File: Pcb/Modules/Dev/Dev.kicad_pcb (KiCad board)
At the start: 2 copper layers, 50.8 x 20.3 mm, 6 parts, among them J1 JACK_STEREO, J2 JACK_RJ45, P1 CONN_02X04, Q1 Q_NMOS_GSD, SW0 SW_TACTILE

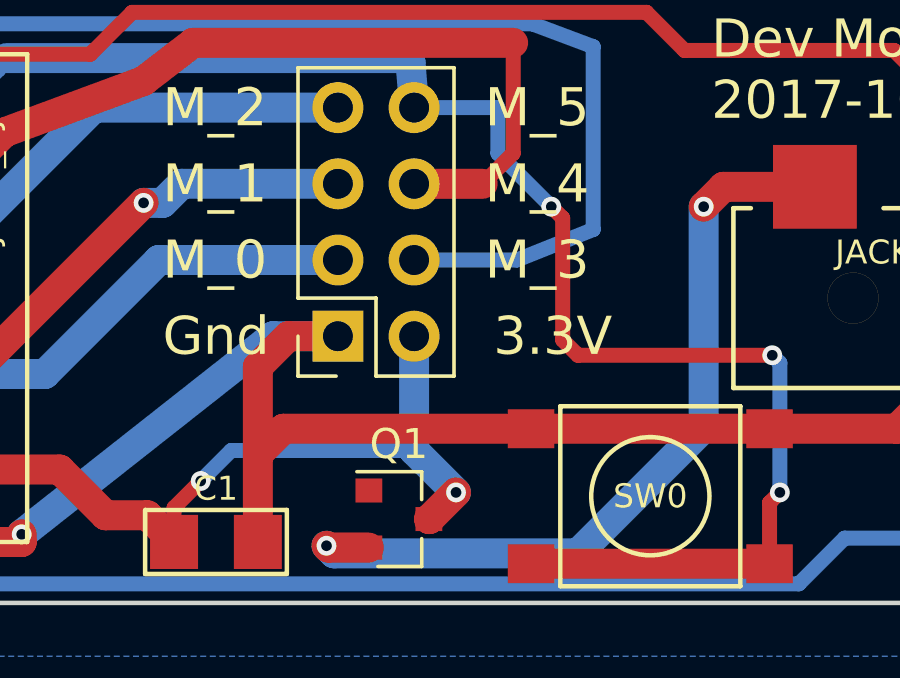
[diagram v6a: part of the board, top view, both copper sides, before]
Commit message: Fix missing wire on dev board and stop rounding corners on light pcb
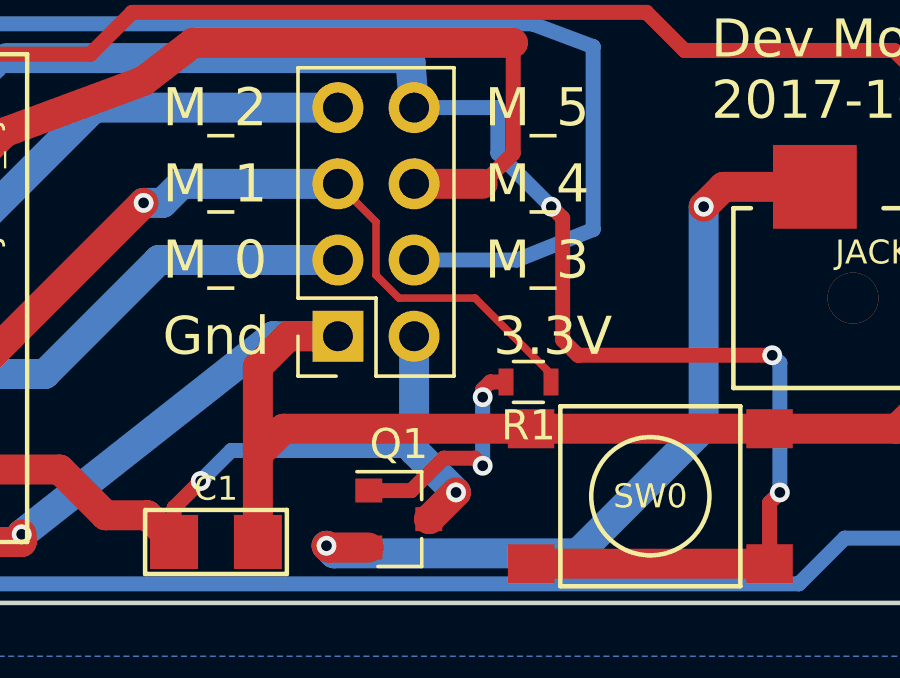
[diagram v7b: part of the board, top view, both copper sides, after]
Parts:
- added R1: 1K, Resistors_SMD:R_0603, F.Cu at (54.6, 38.4)
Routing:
- net /M_1: track 30.4 -> 41.4 mm
- net Net-(Q1-Pad1): track 0.00 -> 7.77 mm, vias 0 -> 2
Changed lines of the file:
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@@
 (kicad_pcb (version 4) (host pcbnew 4.0.5)
   (general
-    (links 20)
+    (links 22)
     (no_connects 0)
-    (area 21.873869 24.13 78.740001 48.768001)
+    (area 25.324999 25.324999 76.275001 45.795001)
     (thickness 1.6)
     (drawings 21)
-    (tracks 137)
+    (tracks 153)
     (zones 0)
-    (modules 6)
+    (modules 7)
     (nets 11)
   )
@@
   )
   (setup
-    (last_trace_width 0.5)
+    (last_trace_width 0.254)
+    (user_trace_width 0.254)
     (trace_clearance 0.2032)
     (zone_clearance 0.508)
@@
     (pad 4 smd rect (at 3.975 2.25) (size 1.55 1.3) (layers F.Cu F.Paste F.Mask)
       (net 9 /M_5))
+  )
+  (module Resistors_SMD:R_0603 (layer F.Cu)
+    (at 54.61 38.354 180)
+    (descr "Resistor SMD 0603, reflow soldering, Vishay (see dcrcw.pdf)")
+    (tags "resistor 0603")
+    (attr smd)
+    (fp_text reference R1 (at 0 -1.45 180) (layer F.SilkS)
+      (effects (font (size 1 1) (thickness 0.15)))
+    )
+    (fp_text value 1K (at 0 1.5 180) (layer F.Fab)
+      (effects (font (size 1 1) (thickness 0.15)))
+    )
+    (fp_text user %R (at 0 0 180) (layer F.Fab)
+      (effects (font (size 0.4 0.4) (thickness 0.075)))
+    )
+    (fp_line (start -0.8 0.4) (end -0.8 -0.4) (layer F.Fab) (width 0.1))
+    (fp_line (start 0.8 0.4) (end -0.8 0.4) (layer F.Fab) (width 0.1))
+    (fp_line (start 0.8 -0.4) (end 0.8 0.4) (layer F.Fab) (width 0.1))
+    (fp_line (start -0.8 -0.4) (end 0.8 -0.4) (layer F.Fab) (width 0.1))
+    (fp_line (start 0.5 0.68) (end -0.5 0.68) (layer F.SilkS) (width 0.12))
+    (fp_line (start -0.5 -0.68) (end 0.5 -0.68) (layer F.SilkS) (width 0.12))
+    (fp_line (start -1.25 -0.7) (end 1.25 -0.7) (layer F.CrtYd) (width 0.05))
+    (fp_line (start -1.25 -0.7) (end -1.25 0.7) (layer F.CrtYd) (width 0.05))
+    (fp_line (start 1.25 0.7) (end 1.25 -0.7) (layer F.CrtYd) (width 0.05))
+    (fp_line (start 1.25 0.7) (end -1.25 0.7) (layer F.CrtYd) (width 0.05))
+    (pad 1 smd rect (at -0.75 0 180) (size 0.5 0.9) (layers F.Cu F.Paste F.Mask)
+      (net 6 /M_1))
+    (pad 2 smd rect (at 0.75 0 180) (size 0.5 0.9) (layers F.Cu F.Paste F.Mask)
+      (net 10 "Net-(Q1-Pad1)"))
+    (model ${KISYS3DMOD}/Resistors_SMD.3dshapes/R_0603.wrl
+      (at (xyz 0 0 0))
+      (scale (xyz 1 1 1))
+      (rotate (xyz 0 0 0))
+    )
   )
   (gr_line (start 76.2 25.4) (end 76.2 31.75) (angle 90) (layer Edge.Cuts) (width 0.15))
@@
   (segment (start 26.797 34.941) (end 26.797 32.258) (width 0.5) (layer F.Cu) (net 5))
   (segment (start 26.678 35.06) (end 26.797 34.941) (width 0.5) (layer F.Cu) (net 5))
-  (segment (start 30.099 41.783) (end 29.845 41.783) (width 0.5) (layer B.Cu) (net 6))
+  (segment (start 55.36 38.354) (end 55.36 38.088) (width 0.254) (layer F.Cu) (net 6))
+  (segment (start 55.36 38.088) (end 52.832 35.56) (width 0.254) (layer F.Cu) (net 6))
+  (segment (start 52.832 35.56) (end 50.292 35.56) (width 0.254) (layer F.Cu) (net 6))
+  (segment (start 50.292 35.56) (end 49.53 34.798) (width 0.254) (layer F.Cu) (net 6))
+  (segment (start 49.53 34.798) (end 49.53 33.02) (width 0.254) (layer F.Cu) (net 6))
+  (segment (start 49.53 33.02) (end 48.26 31.75) (width 0.254) (layer F.Cu) (net 6))
+  (segment (start 48.26 31.75) (end 43.053 31.75) (width 1) (layer B.Cu) (net 6) (status 10))
   (segment (start 43.053 31.75) (end 42.418 32.385) (width 1) (layer B.Cu) (net 6))
   (segment (start 42.418 32.385) (end 41.783 32.385) (width 1) (layer B.Cu) (net 6))
   (via (at 41.783 32.385) (size 0.6604) (drill 0.3556) (layers F.Cu B.Cu) (net 6))
   (segment (start 41.783 32.385) (end 34.671 39.497) (width 1) (layer F.Cu) (net 6))
+  (segment (start 30.099 41.783) (end 29.845 41.783) (width 0.5) (layer B.Cu) (net 6))
   (via (at 34.671 39.497) (size 0.6604) (drill 0.3556) (layers F.Cu B.Cu) (net 6))
   (segment (start 34.671 39.497) (end 32.385 41.783) (width 1) (layer B.Cu) (net 6))
   (segment (start 32.385 41.783) (end 30.099 41.783) (width 1) (layer B.Cu) (net 6))
-  (segment (start 48.26 31.75) (end 43.053 31.75) (width 1) (layer B.Cu) (net 6) (status 10))
   (segment (start 27.819 37.09) (end 30.092 37.09) (width 0.5) (layer F.Cu) (net 6) (status 20))
   (segment (start 27.813 37.084) (end 27.819 37.09) (width 0.5) (layer F.Cu) (net 6))
@@
   (segment (start 50.546 27.559) (end 37.211 27.559) (width 1) (layer B.Cu) (net 9))
   (segment (start 62.649 44.414) (end 54.699 44.414) (width 1) (layer F.Cu) (net 9) (status 30))
+  (segment (start 53.086 38.862) (end 53.086 38.608) (width 0.5) (layer F.Cu) (net 10))
+  (segment (start 49.292 41.976) (end 50.707202 41.976) (width 0.5) (layer F.Cu) (net 10))
+  (via (at 53.086 38.862) (size 0.6604) (drill 0.3556) (layers F.Cu B.Cu) (net 10))
+  (segment (start 53.086 41.148) (end 53.086 38.862) (width 0.5) (layer B.Cu) (net 10))
+  (via (at 53.086 41.148) (size 0.6604) (drill 0.3556) (layers F.Cu B.Cu) (net 10))
+  (segment (start 52.832 40.894) (end 53.086 41.148) (width 0.5) (layer F.Cu) (net 10))
+  (segment (start 51.789202 40.894) (end 52.832 40.894) (width 0.5) (layer F.Cu) (net 10))
+  (segment (start 50.707202 41.976) (end 51.789202 40.894) (width 0.5) (layer F.Cu) (net 10))
+  (segment (start 53.34 38.354) (end 53.86 38.354) (width 0.5) (layer F.Cu) (net 10))
+  (segment (start 53.086 38.608) (end 53.34 38.354) (width 0.5) (layer F.Cu) (net 10))
   (zone (net 2) (net_name GND) (layer F.Cu) (hatch edge 0.508)
     (connect_pads (clearance 0.508))

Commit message: Update PCBs
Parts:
- added R2: 10K, Resistors_SMD:R_0603, F.Cu at (64.8, 43.8)
- added X1: HOLE, Mounting_Holes:MountingHole_2.5mm_Pad, F.Cu at (41.3, 28.6)
- added X2: HOLE, Mounting_Holes:MountingHole_2.5mm_Pad, F.Cu at (41.3, 42.5)
- added X3: HOLE, Mounting_Holes:MountingHole_2.5mm_Pad, F.Cu at (60.3, 28.6)
- added X4: HOLE, Mounting_Holes:MountingHole_2.5mm_Pad, F.Cu at (60.3, 42.5)
- C1: value C -> 10uF
- moved Q1 17.7 mm to (67.9, 42.5)
- moved R1 10.4 mm to (64.8, 40.6), turned to 0 degrees
- moved SW0 7.92 mm to (50.8, 41.3), turned to 180 degrees
- moved C1 6.63 mm to (41.9, 37.5)
- moved P1 2.29 mm to (49.5, 34.9)
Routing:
- net GND: track 113.7 -> 6.63 mm, vias 1 -> 5
- net /M_3: track 52.8 -> 29.3 mm, vias 1 -> 4
- net 3V3: track 32.0 -> 49.0 mm, vias 2 -> 0
- net /M_0: track 63.2 -> 46.6 mm, vias 1 -> 0
- net /M_5: track 59.5 -> 43.6 mm, vias 3 -> 4
- net /M_1: track 41.4 -> 54.1 mm, vias 3 -> 2
- net /M_4: track 32.1 -> 23.0 mm, vias 0 -> 2
- net Net-(Q1-Pad1): track 7.77 -> 1.82 mm, vias 2 -> 0
- net Net-(J1-Pad2): track 27.2 -> 25.0 mm, vias 2 -> 0
- net /M_2: track 20.2 -> 21.3 mm
- removed copper zone on F.Cu, net GND
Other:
- net class Default: trace_width 0.5 -> 0.254
